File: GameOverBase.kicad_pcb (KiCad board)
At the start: 2 copper layers, 40 x 25 mm, 0 parts

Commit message: Changes layer count to 4 on PCB
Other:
- copper layers 2 -> 4
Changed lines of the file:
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@@
   (paper "A4")
   (layers
-    (0 "F.Cu" signal "cobre frontal")
-    (31 "B.Cu" signal "Cobre traseira")
+    (0 "F.Cu" mixed "cobre frontal")
+    (1 "In1.Cu" power)
+    (2 "In2.Cu" power)
+    (31 "B.Cu" mixed "Cobre traseira")
     (32 "B.Adhes" user "Adesivo traseira")
     (33 "F.Adhes" user "Adesivo frontal")
@@
   )
   (setup
+    (stackup
+      (layer "F.SilkS" (type "Top Silk Screen"))
+      (layer "F.Paste" (type "Top Solder Paste"))
+      (layer "F.Mask" (type "Top Solder Mask") (thickness 0.01))
+      (layer "F.Cu" (type "copper") (thickness 0.035))
+      (layer "dielectric 1" (type "prepreg") (thickness 0.48) (material "FR4") (epsilon_r 4.5) (loss_tangent 0.02))
+      (layer "In1.Cu" (type "copper") (thickness 0.035))
+      (layer "dielectric 2" (type "prepreg") (thickness 0.48) (material "FR4") (epsilon_r 4.5) (loss_tangent 0.02))
+      (layer "In2.Cu" (type "copper") (thickness 0.035))
+      (layer "dielectric 3" (type "core") (thickness 0.48) (material "FR4") (epsilon_r 4.5) (loss_tangent 0.02))
+      (layer "B.Cu" (type "copper") (thickness 0.035))
+      (layer "B.Mask" (type "Bottom Solder Mask") (thickness 0.01))
+      (layer "B.Paste" (type "Bottom Solder Paste"))
+      (layer "B.SilkS" (type "Bottom Silk Screen"))
+      (copper_finish "None")
+      (dielectric_constraints no)
+    )
     (pad_to_mask_clearance 0)
     (pcbplotparams

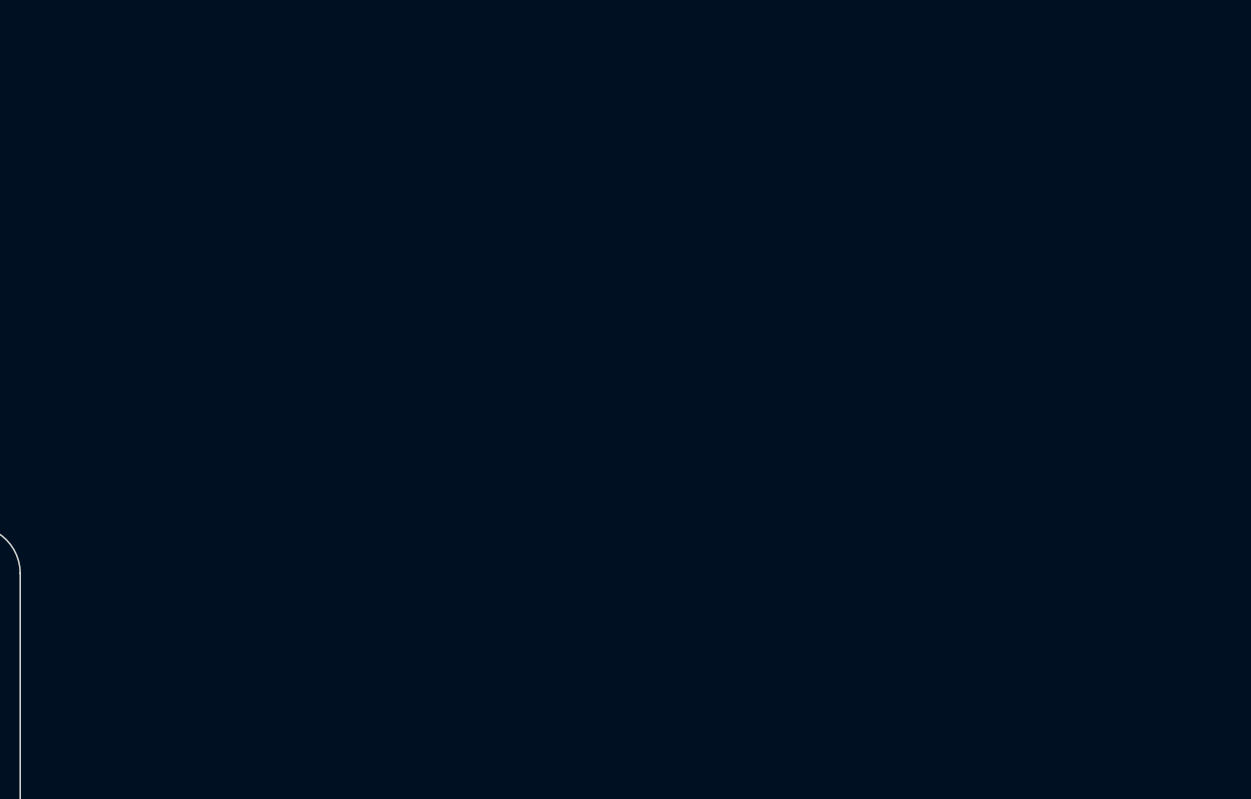
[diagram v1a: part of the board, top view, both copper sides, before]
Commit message: Imports components into the PCB
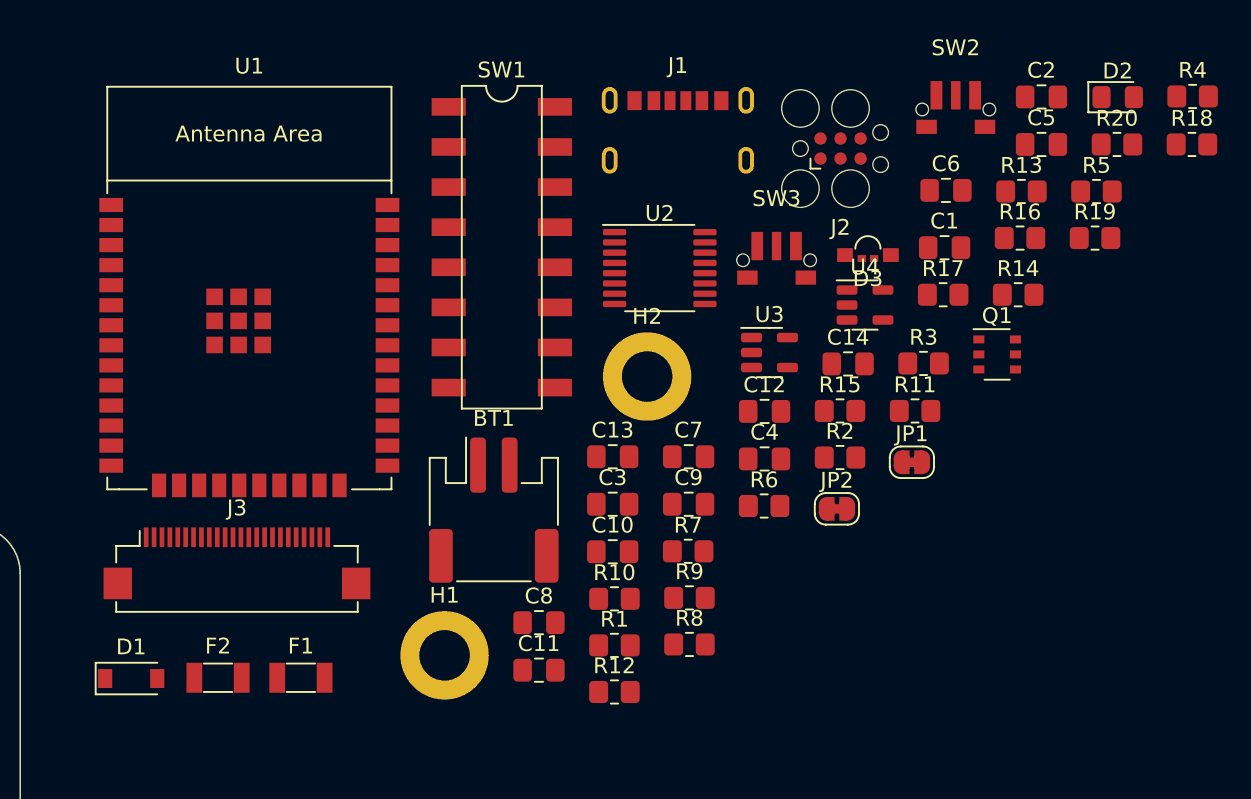
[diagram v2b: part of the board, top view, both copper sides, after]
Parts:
- added BT1: LiPO (protected), Connector_JST:JST_PH_S2B-PH-SM4-TB_1x02-1MP_P2.00mm_Horizontal, F.Cu at (190.0, 79.0)
- added C1: 100nF, Capacitor_SMD:C_0805_2012Metric_Pad1.18x1.45mm_HandSolder, F.Cu at (218.6, 62.4)
- added C10: 100nF, Capacitor_SMD:C_0805_2012Metric_Pad1.18x1.45mm_HandSolder, F.Cu at (197.5, 81.6)
- added C11: 10µF, Capacitor_SMD:C_0805_2012Metric_Pad1.18x1.45mm_HandSolder, F.Cu at (192.9, 89.1)
- added C12: 10µF, Capacitor_SMD:C_0805_2012Metric_Pad1.18x1.45mm_HandSolder, F.Cu at (207.2, 72.8)
- added C13: 100nF, Capacitor_SMD:C_0805_2012Metric_Pad1.18x1.45mm_HandSolder, F.Cu at (197.5, 75.6)
- added C14: 10µF, Capacitor_SMD:C_0805_2012Metric_Pad1.18x1.45mm_HandSolder, F.Cu at (212.4, 69.7)
- added C2: 100nF, Capacitor_SMD:C_0805_2012Metric_Pad1.18x1.45mm_HandSolder, F.Cu at (224.7, 52.8)
- added C3: 10µF, Capacitor_SMD:C_0805_2012Metric_Pad1.18x1.45mm_HandSolder, F.Cu at (197.5, 78.6)
- added C4: 1µF, Capacitor_SMD:C_0805_2012Metric_Pad1.18x1.45mm_HandSolder, F.Cu at (207.2, 75.8)
- added C5: 100nF, Capacitor_SMD:C_0805_2012Metric_Pad1.18x1.45mm_HandSolder, F.Cu at (224.7, 55.8)
- added C6: 100nF, Capacitor_SMD:C_0805_2012Metric_Pad1.18x1.45mm_HandSolder, F.Cu at (218.6, 58.8)
- added C7: 100nF, Capacitor_SMD:C_0805_2012Metric_Pad1.18x1.45mm_HandSolder, F.Cu at (202.3, 75.6)
- added C8: 100nF, Capacitor_SMD:C_0805_2012Metric_Pad1.18x1.45mm_HandSolder, F.Cu at (192.9, 86.1)
- added C9: 100nF, Capacitor_SMD:C_0805_2012Metric_Pad1.18x1.45mm_HandSolder, F.Cu at (202.3, 78.6)
- added D1: MBR120, Diode_SMD:D_SOD-123, F.Cu at (167.0, 89.7)
- added D2: green, LED_SMD:LED_0805_2012Metric_Pad1.15x1.40mm_HandSolder, F.Cu at (229.5, 52.8)
- added D3: LED_RGBA, GameOver:Hongzhi_Forest_HS-1204-RGB, F.Cu at (213.7, 62.8)
- added F1: PTC 1A, GameOver:Belfuse_0ZCJ, F.Cu at (177.8, 89.6)
- added F2: PTC 1A, GameOver:Belfuse_0ZCJ, F.Cu at (172.5, 89.6)
- added H1: ~, MountingHole:MountingHole_3.2mm_M3_DIN965_Pad, F.Cu at (186.9, 88.2)
- added H2: ~, MountingHole:MountingHole_3.2mm_M3_DIN965_Pad, F.Cu at (199.7, 70.5)
- added J1: USB_C_DEALON-USB-US31-106, GameOver:DEALON_USB-US31-106, F.Cu at (201.7, 55.9)
- added J2: Serial Port, Connector:Tag-Connect_TC2030-IDC-FP_2x03_P1.27mm_Vertical, F.Cu at (212.0, 56.1)
- added J3: add-on conn, GameOver:TXGA_FFC05036-24SBD113W5M_1x24_P0.50mm_Horizontal, F.Cu at (173.7, 82.6)
- added JP1: ~, Jumper:SolderJumper-2_P1.3mm_Bridged_RoundedPad1.0x1.5mm, F.Cu at (216.5, 76.0)
- added JP2: ~, Jumper:SolderJumper-2_P1.3mm_Bridged_RoundedPad1.0x1.5mm, F.Cu at (211.7, 78.9)
- added Q1: PMN48XP, Package_SO:TSOP-6_1.65x3.05mm_P0.95mm, F.Cu at (221.9, 69.1)
- added R1: 10kΩ, Resistor_SMD:R_0805_2012Metric_Pad1.20x1.40mm_HandSolder, F.Cu at (197.6, 87.6)
- added R10: 10kΩ, Resistor_SMD:R_0805_2012Metric_Pad1.20x1.40mm_HandSolder, F.Cu at (197.6, 84.6)
- added R11: 10kΩ, Resistor_SMD:R_0805_2012Metric_Pad1.20x1.40mm_HandSolder, F.Cu at (216.7, 72.7)
- added R12: 10kΩ, Resistor_SMD:R_0805_2012Metric_Pad1.20x1.40mm_HandSolder, F.Cu at (197.6, 90.5)
- added R13: 100kΩ, Resistor_SMD:R_0805_2012Metric_Pad1.20x1.40mm_HandSolder, F.Cu at (223.4, 58.8)
- added R14: 100kΩ, Resistor_SMD:R_0805_2012Metric_Pad1.20x1.40mm_HandSolder, F.Cu at (223.2, 65.4)
- added R15: 10k, Resistor_SMD:R_0805_2012Metric_Pad1.20x1.40mm_HandSolder, F.Cu at (211.9, 72.7)
- added R16: 5.1kΩ *, Resistor_SMD:R_0805_2012Metric_Pad1.20x1.40mm_HandSolder, F.Cu at (223.3, 61.8)
- added R17: 1kΩ, Resistor_SMD:R_0805_2012Metric_Pad1.20x1.40mm_HandSolder, F.Cu at (218.5, 65.4)
- added R18: 1kΩ, Resistor_SMD:R_0805_2012Metric_Pad1.20x1.40mm_HandSolder, F.Cu at (234.2, 55.8)
- added R19: 1kΩ, Resistor_SMD:R_0805_2012Metric_Pad1.20x1.40mm_HandSolder, F.Cu at (228.1, 61.8)
- added R2: 10kΩ, Resistor_SMD:R_0805_2012Metric_Pad1.20x1.40mm_HandSolder, F.Cu at (211.9, 75.7)
- added R20: 1kΩ, Resistor_SMD:R_0805_2012Metric_Pad1.20x1.40mm_HandSolder, F.Cu at (229.5, 55.8)
- added R3: 5.1kΩ, Resistor_SMD:R_0805_2012Metric_Pad1.20x1.40mm_HandSolder, F.Cu at (217.2, 69.7)
- added R4: 5.1kΩ, Resistor_SMD:R_0805_2012Metric_Pad1.20x1.40mm_HandSolder, F.Cu at (234.3, 52.8)
- added R5: 10kΩ, Resistor_SMD:R_0805_2012Metric_Pad1.20x1.40mm_HandSolder, F.Cu at (228.2, 58.8)
- added R6: 10kΩ, Resistor_SMD:R_0805_2012Metric_Pad1.20x1.40mm_HandSolder, F.Cu at (207.1, 78.7)
- added R7: 10kΩ, Resistor_SMD:R_0805_2012Metric_Pad1.20x1.40mm_HandSolder, F.Cu at (202.3, 81.6)
- added R8: 10kΩ, Resistor_SMD:R_0805_2012Metric_Pad1.20x1.40mm_HandSolder, F.Cu at (202.4, 87.5)
- added R9: 10kΩ, Resistor_SMD:R_0805_2012Metric_Pad1.20x1.40mm_HandSolder, F.Cu at (202.4, 84.6)
- added SW1: SW_DIP_x08, GameOver:DIP-16_CTS_219-8LPST, F.Cu at (190.5, 62.4)
- added SW2: boot, GameOver:SW_Tactile_SPST_SOFNG_TS-1814, F.Cu at (219.3, 52.7)
- added SW3: Reset, GameOver:SW_Tactile_SPST_SOFNG_TS-1814, F.Cu at (207.9, 62.3)
- added U1: ESP32-WROOM-E, Espressif:ESP32-WROOM-32E, F.Cu at (174.5, 66.7)
- added U2: 4021, Package_SO:TSSOP-16_4.4x5mm_P0.65mm, F.Cu at (200.5, 63.7)
- added U3: MCP73831-2ACI-OT, Package_TO_SOT_SMD:SOT-23-5, F.Cu at (207.5, 69.0)
- added U4: XC6210B332MR, Package_TO_SOT_SMD:SOT-23-5, F.Cu at (213.5, 66.0)

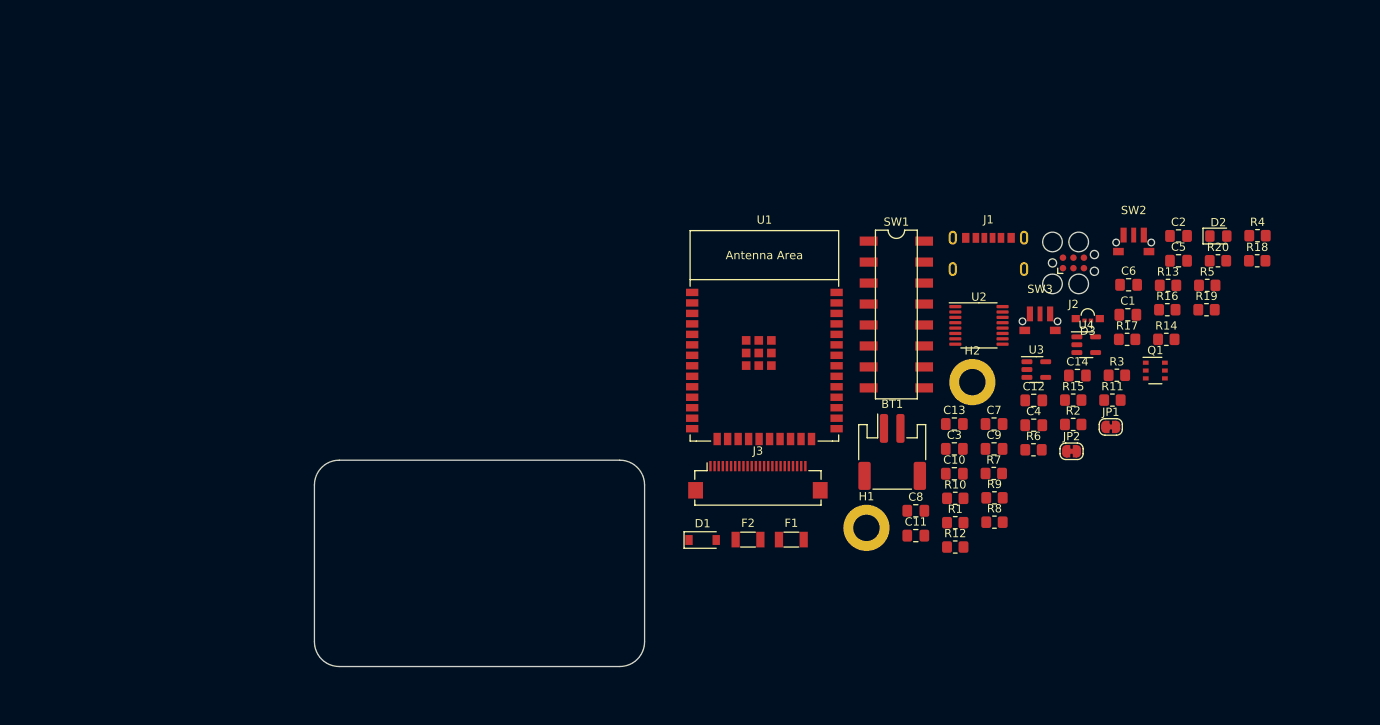
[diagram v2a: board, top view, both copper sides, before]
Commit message: Increases PCB dimensions slightly
It's now 50mm x 30mm.
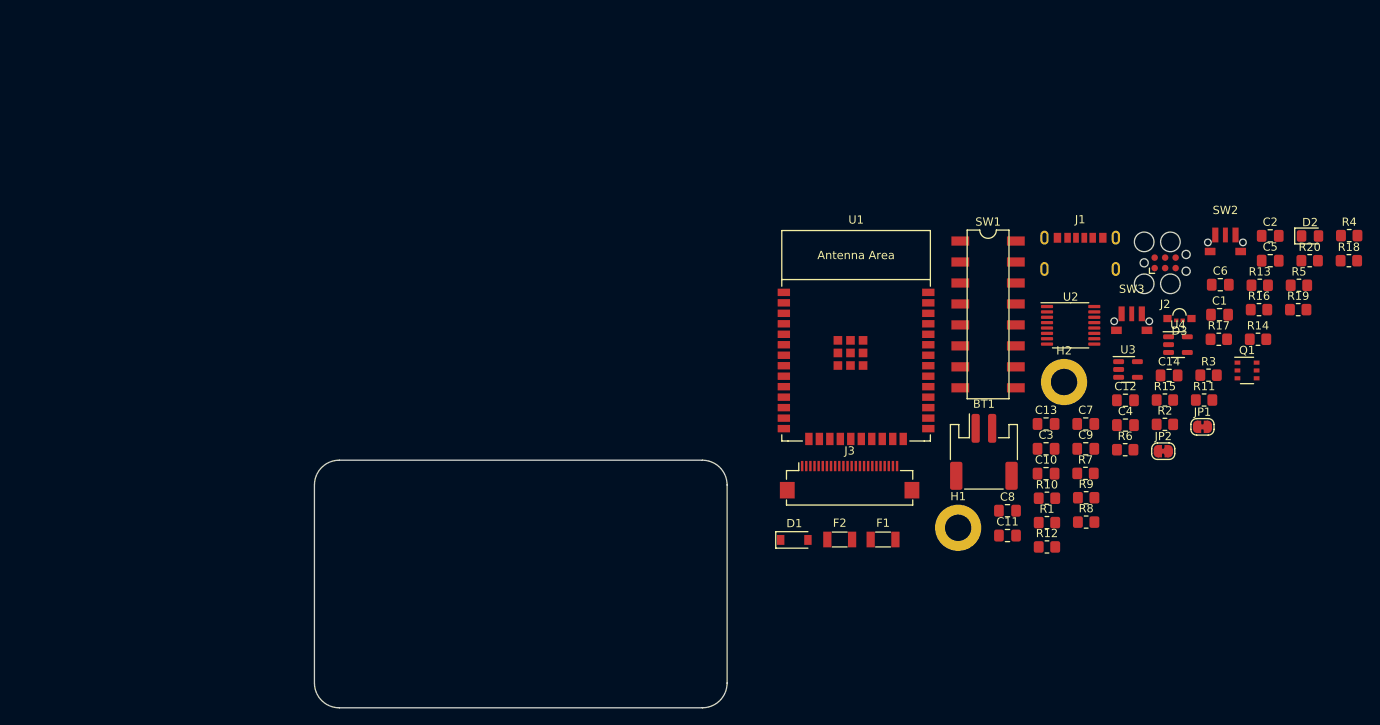
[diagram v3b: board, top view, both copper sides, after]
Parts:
- moved BT1 11.1 mm to (201.1, 79.0)
- moved C14 11.1 mm to (223.6, 69.7)
- moved C2 11.1 mm to (235.8, 52.8)
- moved C5 11.1 mm to (235.8, 55.8)
- moved C6 11.1 mm to (229.8, 58.7)
- moved D2 11.1 mm to (240.6, 52.8)
- moved D3 11.1 mm to (224.8, 62.8)
- moved H1 11.1 mm to (198.0, 88.2)
- moved J1 11.1 mm to (212.8, 55.8)
- moved J3 11.1 mm to (184.8, 82.6)
- moved JP1 11.1 mm to (227.6, 76.0)
- moved JP2 11.1 mm to (222.8, 78.9)
- moved Q1 11.1 mm to (233.0, 69.1)
- moved R1 11.1 mm to (208.8, 87.6)
- moved R10 11.1 mm to (208.8, 84.6)
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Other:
- board size 40 x 25 mm -> 50 x 30 mm

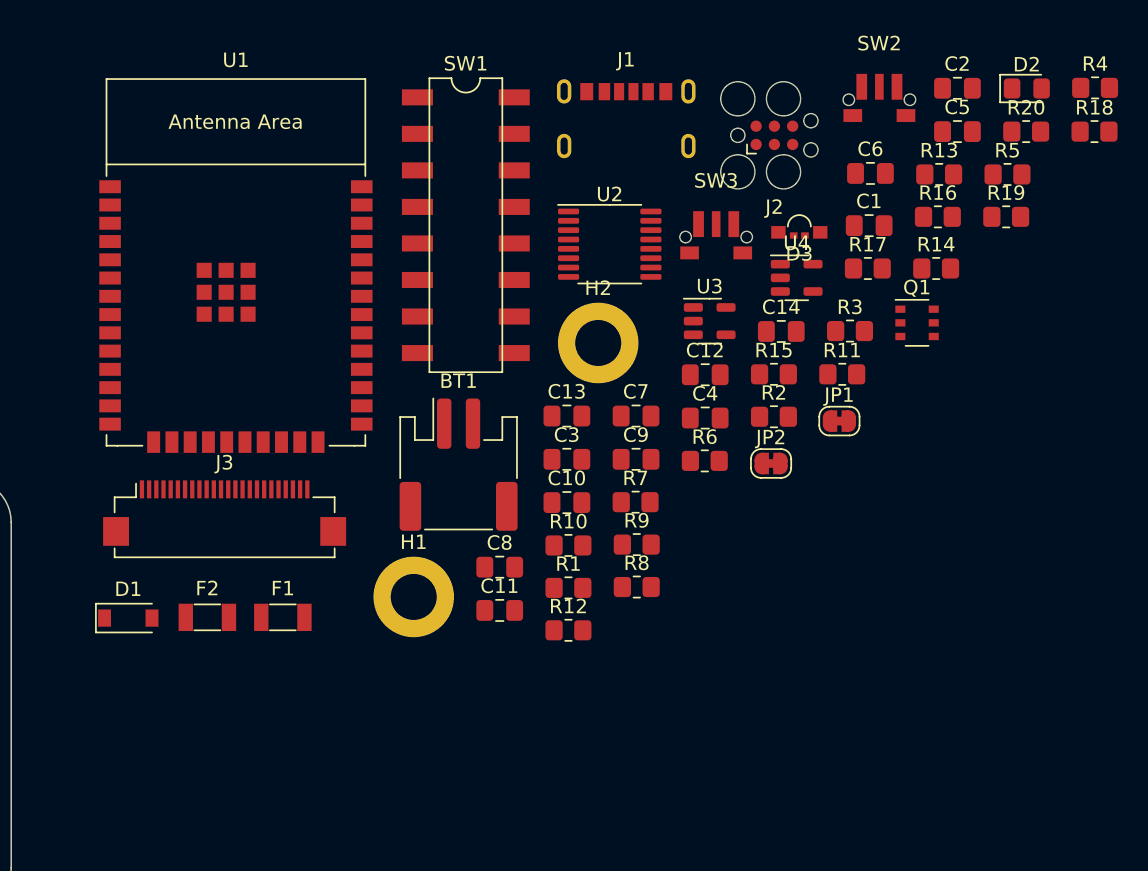
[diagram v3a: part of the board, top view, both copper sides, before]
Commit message: Updates PCB footprints after adding resistor network and removing charging led
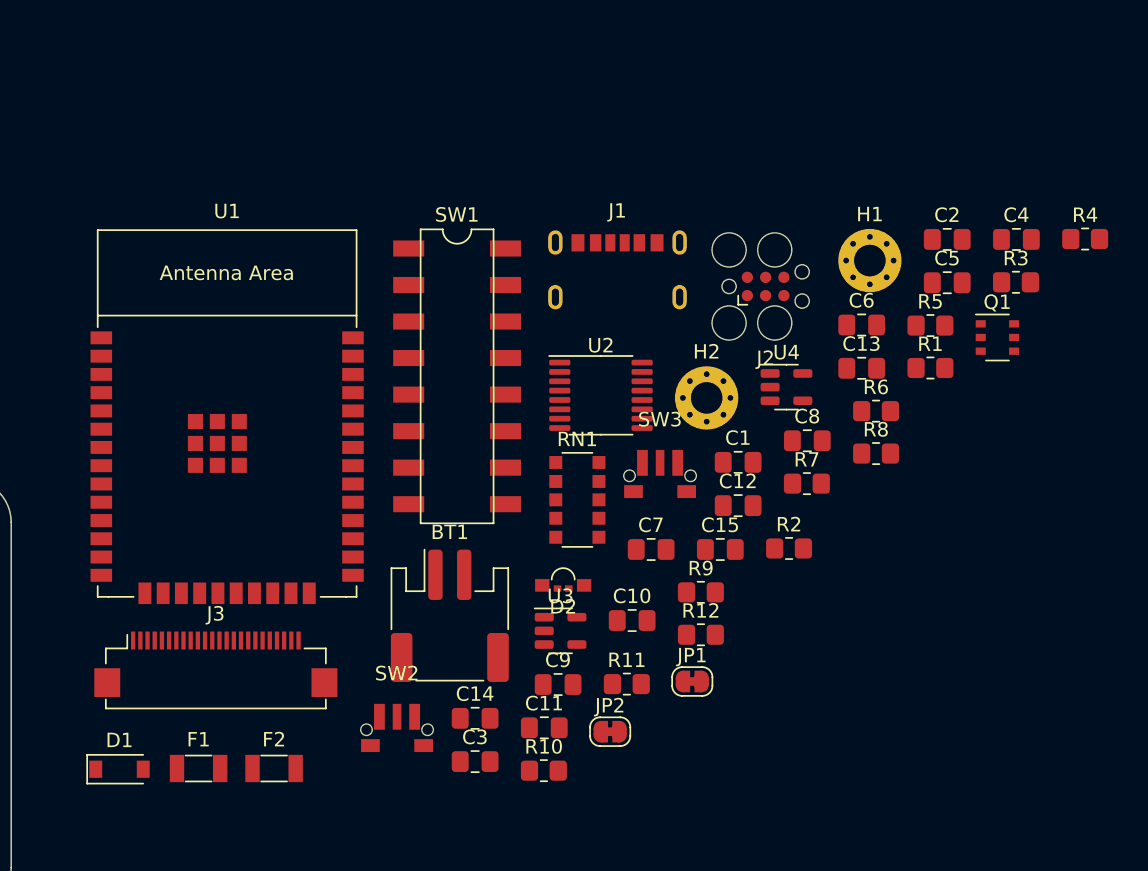
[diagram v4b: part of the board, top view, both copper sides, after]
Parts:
- removed D3: LED_RGBA, GameOver:Hongzhi_Forest_HS-1204-RGB
- removed R13, R14: 100kΩ, Resistor_SMD:R_0805_2012Metric_Pad1.20x1.40mm_HandSolder
- removed R15: 10k, Resistor_SMD:R_0805_2012Metric_Pad1.20x1.40mm_HandSolder
- removed R16: 5.1kΩ *, Resistor_SMD:R_0805_2012Metric_Pad1.20x1.40mm_HandSolder
- removed R17, R18, R19, R20: 1kΩ, Resistor_SMD:R_0805_2012Metric_Pad1.20x1.40mm_HandSolder
- added C15: 10µF, Capacitor_SMD:C_0805_2012Metric_Pad1.18x1.45mm_HandSolder, F.Cu at (219.3, 84.9)
- added RN1: R_Network08_US, Resistor_SMD:R_Array_Convex_5x1206, F.Cu at (209.4, 81.4)
- C11, C14: value 10µF -> 100nF
- C13: value 100nF -> 10µF
- D2: value green -> LED_RGBA; footprint LED_SMD:LED_0805_2012Metric_Pad1.15x1.40mm_HandSolder -> GameOver:Hongzhi_Forest_HS-1204-RGB
- H1, H2: footprint MountingHole:MountingHole_3.2mm_M3_DIN965_Pad -> MountingHole:MountingHole_2.2mm_M2_Pad_Via
- R10, R11, R12: value 10kΩ -> 1kΩ
- R5, R6: value 10kΩ -> 100kΩ
- R7: value 10kΩ -> 10k
- R8: value 10kΩ -> 5.1kΩ *
- moved SW2 55.2 mm to (196.8, 96.5)
- moved D2 47.3 mm to (208.4, 87.4)
- moved H1 39.4 mm to (229.7, 64.8)
- moved C14 34.3 mm to (202.3, 96.6)
- moved R1 29.5 mm to (233.9, 72.3)
- moved R11 26.2 mm to (212.8, 94.2)
- moved C4 25.0 mm to (239.9, 63.3)
- moved U3 23.9 mm to (208.2, 90.5)
- moved C8 23.1 mm to (225.4, 77.3)
- moved C3 22.0 mm to (202.3, 99.6)
- moved JP2 21.7 mm to (211.7, 97.6)
- moved JP1 20.8 mm to (217.4, 94.1)
- moved C13 20.8 mm to (229.1, 72.3)
- moved R8 19.1 mm to (230.1, 78.2)
- moved C1 18.8 mm to (220.6, 78.8)
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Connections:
- C11 pad 1: VCC -> +3V3
- C12 pad 1: +BATT -> VCC
- C14 pad 1: +3V3 -> +BATT
- D2 pad 1: GND -> Net-(D2-RK)
- D2 pad 2: Net-(D2-A) -> Net-(D2-GK)
- J3 pad 17: IO32 -> +3V3
- J3 pad 19: IO33 -> IO32
- J3 pad 20: IO34 -> IO33
- J3 pad 21: IO35 -> IO34
- J3 pad 22: IO39 -> IO35
- R10 pad 1: Net-(U2-D5) -> BAT_IND_R
- R10 pad 2: GND -> Net-(D2-RK)
- R11 pad 1: Net-(U2-D6) -> BAT_IND_G
- R11 pad 2: GND -> Net-(D2-GK)
- R12 pad 1: Net-(U2-D7) -> BAT_IND_B
- R12 pad 2: GND -> Net-(D2-BK)
- R5 pad 1: Net-(U2-D0) -> +BATT
- R5 pad 2: GND -> BAT_SENSE
- R6 pad 1: Net-(U2-D1) -> BAT_SENSE
- R7 pad 1: Net-(U2-D2) -> +5V
- R8 pad 1: Net-(U2-D3) -> Net-(U3-PROG)
- R9 pad 1: Net-(U2-D4) -> +3V3
- R9 pad 2: GND -> BAT_STAT
- SW1 pad 10: Net-(U2-D6) -> Net-(RN1-R2)
- SW1 pad 11: Net-(U2-D5) -> Net-(RN1-R3)
- SW1 pad 12: Net-(U2-D4) -> Net-(RN1-R4)
- SW1 pad 13: Net-(U2-D3) -> Net-(RN1-R5)
- SW1 pad 14: Net-(U2-D2) -> Net-(RN1-R6)
- SW1 pad 15: Net-(U2-D1) -> Net-(RN1-R7)
- SW1 pad 16: Net-(U2-D0) -> Net-(RN1-R8)
- SW1 pad 9: Net-(U2-D7) -> Net-(RN1-R1)
- U1 pad 5: IO39 -> BAT_STAT
- U2 pad 1: Net-(U2-D7) -> Net-(RN1-R1)
- U2 pad 13: Net-(U2-D4) -> Net-(RN1-R4)
- U2 pad 14: Net-(U2-D5) -> Net-(RN1-R3)
- U2 pad 15: Net-(U2-D6) -> Net-(RN1-R2)
- U2 pad 4: Net-(U2-D3) -> Net-(RN1-R5)
- U2 pad 5: Net-(U2-D2) -> Net-(RN1-R6)
- U2 pad 6: Net-(U2-D1) -> Net-(RN1-R7)
- U2 pad 7: Net-(U2-D0) -> Net-(RN1-R8)
- U3 pad 1: Net-(U3-STAT) -> BAT_STAT
